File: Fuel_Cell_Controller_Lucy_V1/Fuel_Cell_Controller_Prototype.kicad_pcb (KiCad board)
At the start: 2 copper layers, 100 x 73 mm, 152 parts, among them J1 STD_PWR_HEADER, J2 Conn_02x05_Odd_Even, J3 DE9_Receptacle, J4 DA15_Receptacle_MountingHoles, J5 USB_B_Micro, J6 Screw_Terminal_01x02, J7 OLED, J8 Screw_Terminal_01x02, Q1 SI2302A-TPMSCT-ND, Q2 SI2302A-TPMSCT-ND, Q3 FMMT491ATA, Q4 FMMT491ATA, SW1 PTS815 SJM 250 SMTR LFS, SW2 PTS815 SJM 250 SMTR LFS, U1 LD39050PU33R, U10 FT234XD-R, U11 MCP2542FD-E/SN, U12 USBLC6-2SC6, U13 EL3H7(B)(TA)-VG, U14 MCP602-E/SN, U15 ADS1115IRUGR, U16 ADS1115IRUGR, U17 AD8603, U18 LIS3DHTR, U2 LD39050PU33R, U3 STM32L432KCUx, U4 MAX14572, U5 MAX14572, U6 EL3H7(B)(TA)-VG, U7 MCP1501-33E/SN, U8 AD8603, U9 AD8603, X1 OXETDLJANF-8MHZ

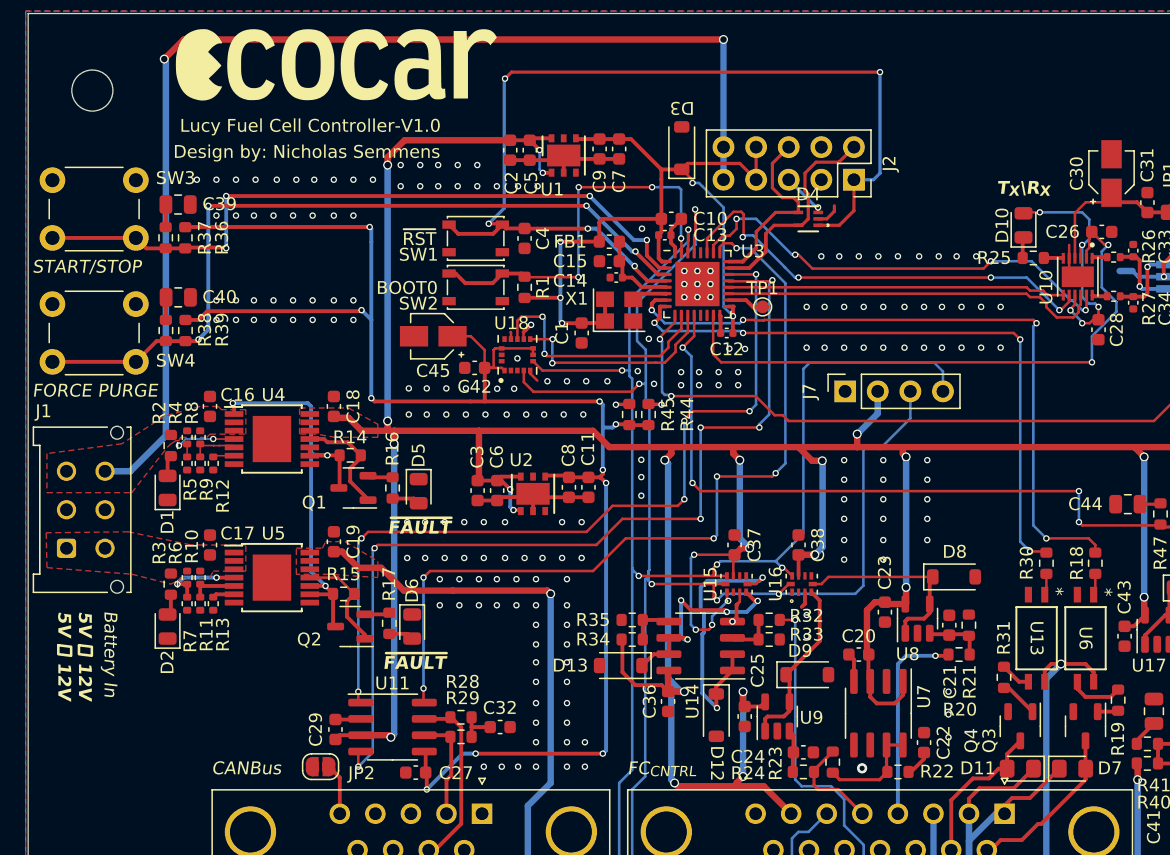
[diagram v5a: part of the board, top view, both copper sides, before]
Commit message: Made some changes to the SWD
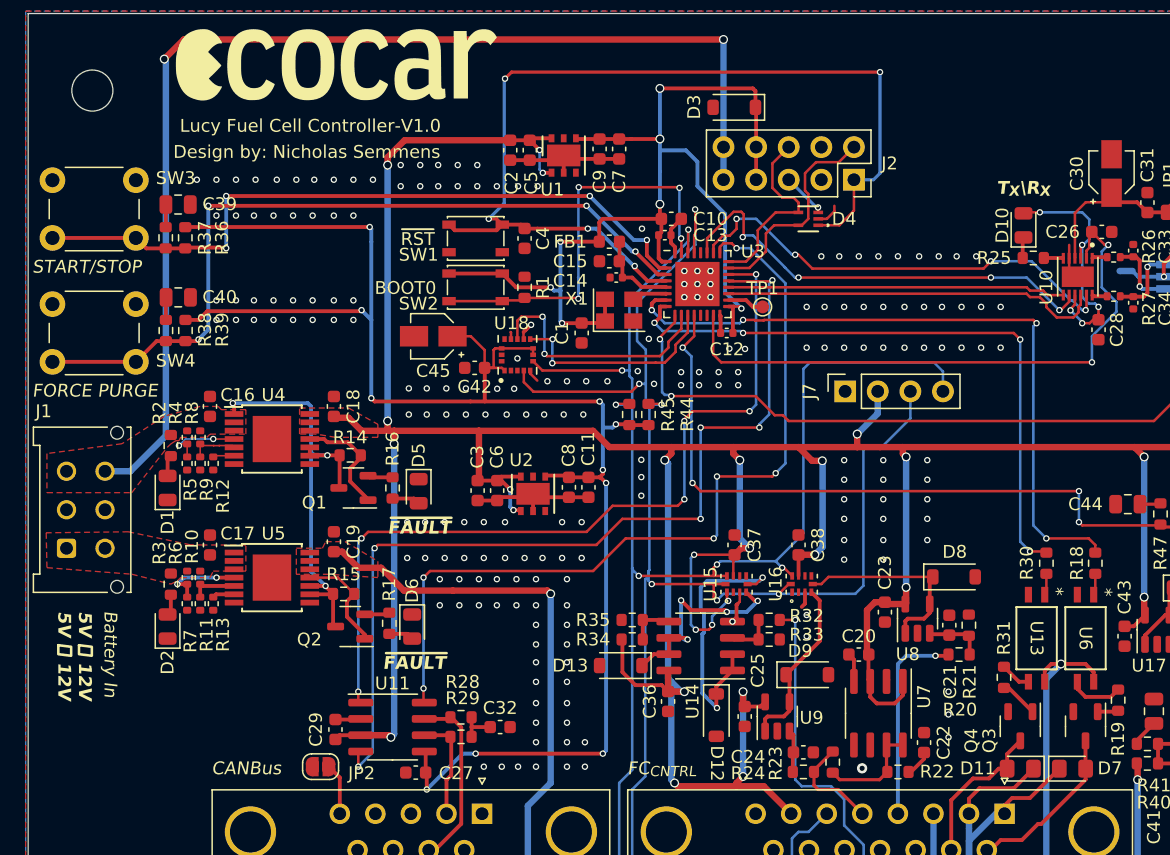
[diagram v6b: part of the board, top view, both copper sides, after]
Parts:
- moved D3 5.26 mm to (154.1, 70.4), turned to 180 degrees
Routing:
- net /MCU_3V3: track 66.1 -> 85.0 mm, vias 5 -> 7
- net /BOOT0: track 30.9 -> 33.6 mm

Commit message: $
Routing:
- net GNDA: vias 218 -> 679

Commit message: I think it is done
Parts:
- removed C32: 4u7, Capacitor_SMD:C_0603_1608Metric
- removed R11: 226k, Resistor_SMD:R_0402_1005Metric
- removed R12, R13: 11.5k, Resistor_SMD:R_0402_1005Metric
- removed R29: 60.4, Resistor_SMD:R_0603_1608Metric
- removed U5: MAX14572, Package_SO:TSSOP-14-1EP_4.4x5mm_P0.65mm
- added C46: 2n2, Capacitor_SMD:C_0603_1608Metric, F.Cu at (114.6, 106.0)
- added C47: 2n2, Capacitor_SMD:C_0603_1608Metric, F.Cu at (114.7, 93.7)
- added U19: TPS259621, Package_SO:TI_SO-PowerPAD-8, F.Cu at (119.6, 107.8)
- R10: value 2.2M -> 909; footprint Resistor_SMD:R_0402_1005Metric -> Resistor_SMD:R_0603_1608Metric
- R28: value 60.4 -> 120
- R4, R6: value 2.2M -> 931; footprint Resistor_SMD:R_0402_1005Metric -> Resistor_SMD:R_0603_1608Metric
- R5: value 953k -> 931; footprint Resistor_SMD:R_0402_1005Metric -> Resistor_SMD:R_0603_1608Metric
- R7: value 267k -> 931; footprint Resistor_SMD:R_0402_1005Metric -> Resistor_SMD:R_0603_1608Metric
- R8: value 2.2M -> 400k; footprint Resistor_SMD:R_0402_1005Metric -> Resistor_SMD:R_0603_1608Metric
- R9: value 549k -> 909; footprint Resistor_SMD:R_0402_1005Metric -> Resistor_SMD:R_0603_1608Metric
- U4: value MAX14572 -> TPS259621; footprint Package_SO:TSSOP-14-1EP_4.4x5mm_P0.65mm -> Package_SO:TI_SO-PowerPAD-8
- moved R10 18.7 mm to (125.8, 94.0), turned to -90 degrees
- moved D6 16.7 mm to (112.5, 114.0), turned to 90 degrees
- moved R9 14.7 mm to (124.5, 106.3), turned to -90 degrees
- moved R17 13.2 mm to (114.3, 113.8), turned to -90 degrees
- moved R8 12.4 mm to (124.3, 92.7), turned to -90 degrees
- moved Q2 7.40 mm to (117.2, 113.5), turned to 0 degrees
- moved D1 6.48 mm to (109.8, 93.5), turned to -90 degrees
- moved C19 5.91 mm to (126.2, 109.0)
- moved R15 5.71 mm to (120.1, 112.8), turned to -90 degrees
- moved C18 5.53 mm to (121.9, 99.1), turned to 0 degrees
- moved R14 5.20 mm to (127.8, 101.1)
- moved D2 4.97 mm to (109.8, 105.8), turned to -90 degrees
- moved C17 4.94 mm to (111.6, 109.1)
- moved R5 4.67 mm to (113.1, 93.7), turned to -90 degrees
- moved C16 3.53 mm to (111.6, 96.8)
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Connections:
- net Net-(Q2-G) renamed /FLT_{12}
- Q1 pad 1: Net-(Q1-G) -> /FLT_{5}
- R10 pad 1: Net-(U5-OVLO) -> GNDA
- R10 pad 2: UNPROTECTED_12V -> Net-(U4-ILM)
- R14 pad 1: Net-(Q1-G) -> /FLT_{5}
- R28 pad 1: Net-(C32-Pad2) -> /IO /CAN_L
- R4 pad 1: Net-(U4-UVLO) -> Net-(U4-EN/UVLO)
- R5 pad 2: Net-(U4-UVLO) -> Net-(U4-EN/UVLO)
- R8 pad 1: Net-(U4-OVLO) -> GNDA
- R8 pad 2: UNPROTECTED_5V -> Net-(U4-OVLO)
- R9 pad 2: Net-(U4-OVLO) -> Net-(U19-ILM)
- U4 pad 1: UNPROTECTED_5V -> GNDA
- U4 pad 2: UNPROTECTED_5V -> Net-(U4-dV/dT)
- U4 pad 3: UNPROTECTED_5V -> Net-(U4-EN/UVLO)
- U4 pad 4: Net-(U4-UVLO) -> UNPROTECTED_5V
- U4 pad 5: Net-(U4-OVLO) -> +5V
- U4 pad 6: Net-(U4-SETI) -> /FLT_{5}
- U4 pad 7: GNDA -> Net-(U4-ILM)
- U4 pad 8: GNDA -> Net-(U4-OVLO)
- U4 pad 9: UNPROTECTED_5V -> GNDA
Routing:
- net /FLT_{5}: track 0.00 -> 14.1 mm, vias 0 -> 2
- net Net-(Q1-G): track 8.91 -> 0.00 mm
- net UNPROTECTED_5V: track 125.7 -> 134.4 mm, vias 5 -> 4
- net Net-(U4-UVLO): track 6.22 -> 0.00 mm, vias 2 -> 0
- net Net-(U4-EN/UVLO): track 0.00 -> 5.05 mm
- net /FLT_{12}: track 8.29 -> 13.1 mm, vias 0 -> 2
- net Net-(U5-OVLO): track 3.71 -> 0.00 mm
- net Net-(U4-ILM): track 0.00 -> 3.60 mm
- net Net-(C32-Pad2): track 3.21 -> 0.00 mm
- net +5V: track 321.6 -> 324.3 mm
- net +3V3: track 129.5 -> 126.9 mm
- net Net-(U19-dV/dT): track 0.00 -> 2.36 mm
- net Net-(U4-dV/dT): track 0.00 -> 2.20 mm
- net Net-(U19-ILM): track 0.00 -> 2.17 mm
- net Net-(U5-SETI): track 1.71 -> 0.00 mm
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- removed copper zone on F.Cu, net +12V
- removed copper zone on F.Cu, net +5V
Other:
- outline, holes or cut-outs redrawn
- board text added: "Issued: ${ISSUE_DATE}"
- board text added: "PURGE"
- board text added: "SWD"
- board text removed: "FORCE PURGE"
